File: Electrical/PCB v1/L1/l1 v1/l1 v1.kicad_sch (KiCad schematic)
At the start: 167 parts, among them J1 Conn_01x01_Socket, J2 Conn_01x01_Socket, SW1 SW_SPDT, U1 ESP32-S3-DEVKITM-1-N8, U2 LM2596ADJ

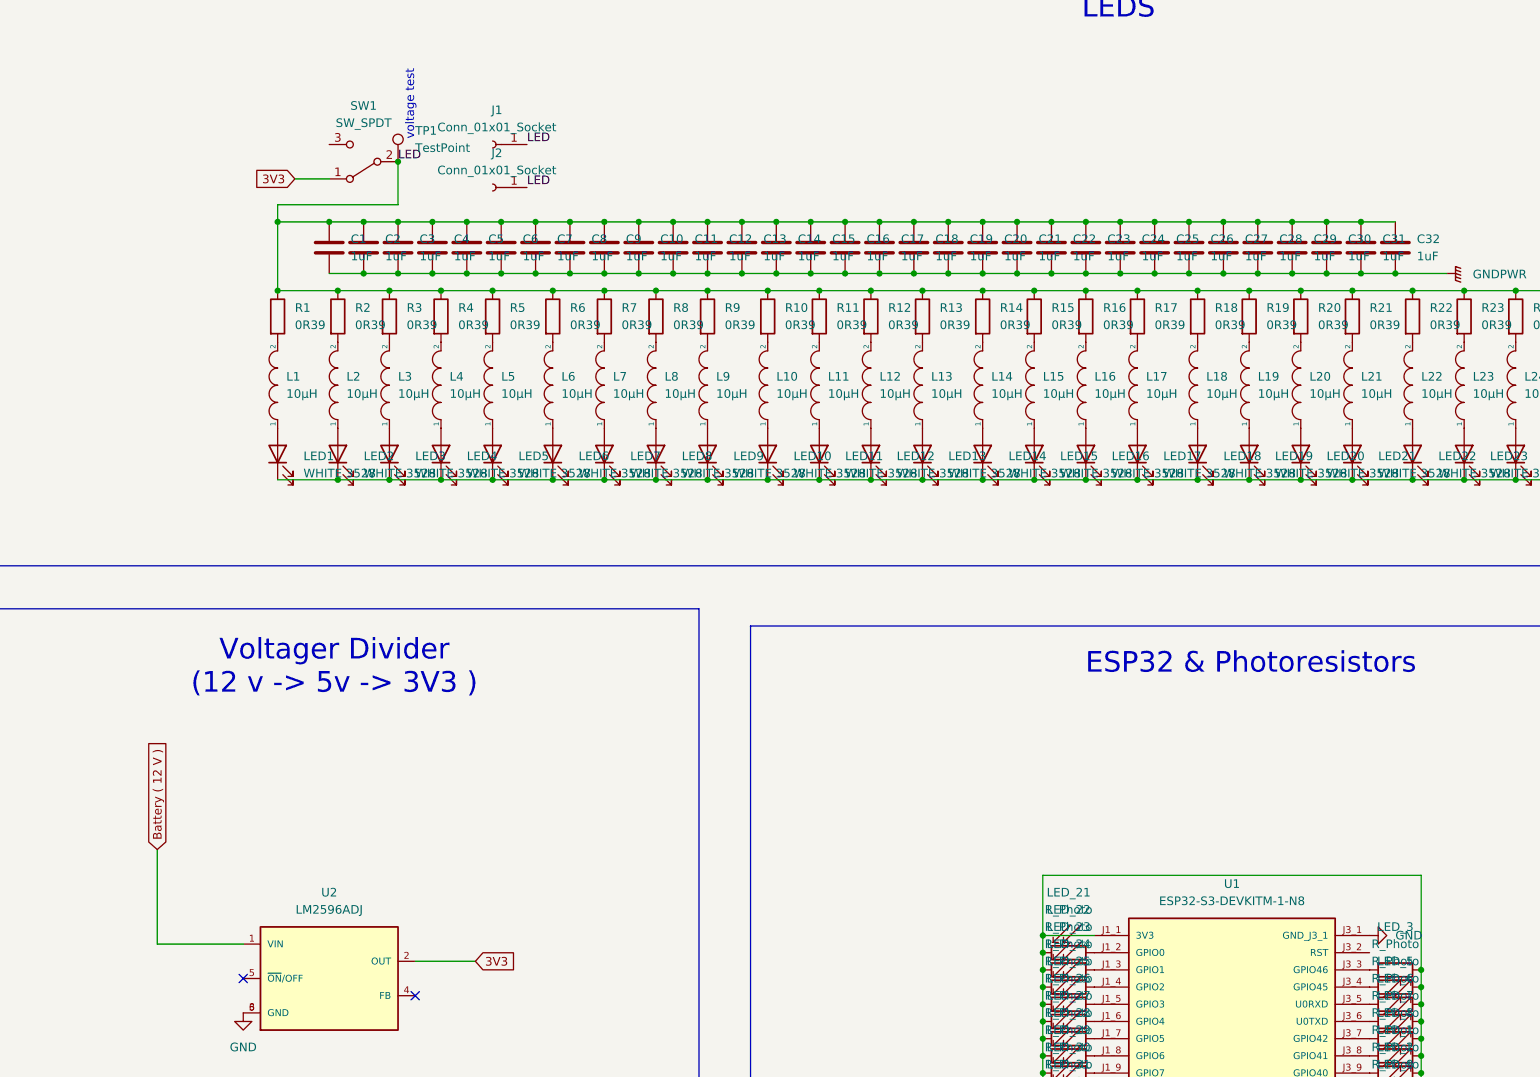
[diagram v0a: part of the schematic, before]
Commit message: renamed volatage divider to dc -dc converted for accurate naming, moved some text around becuz easier to read
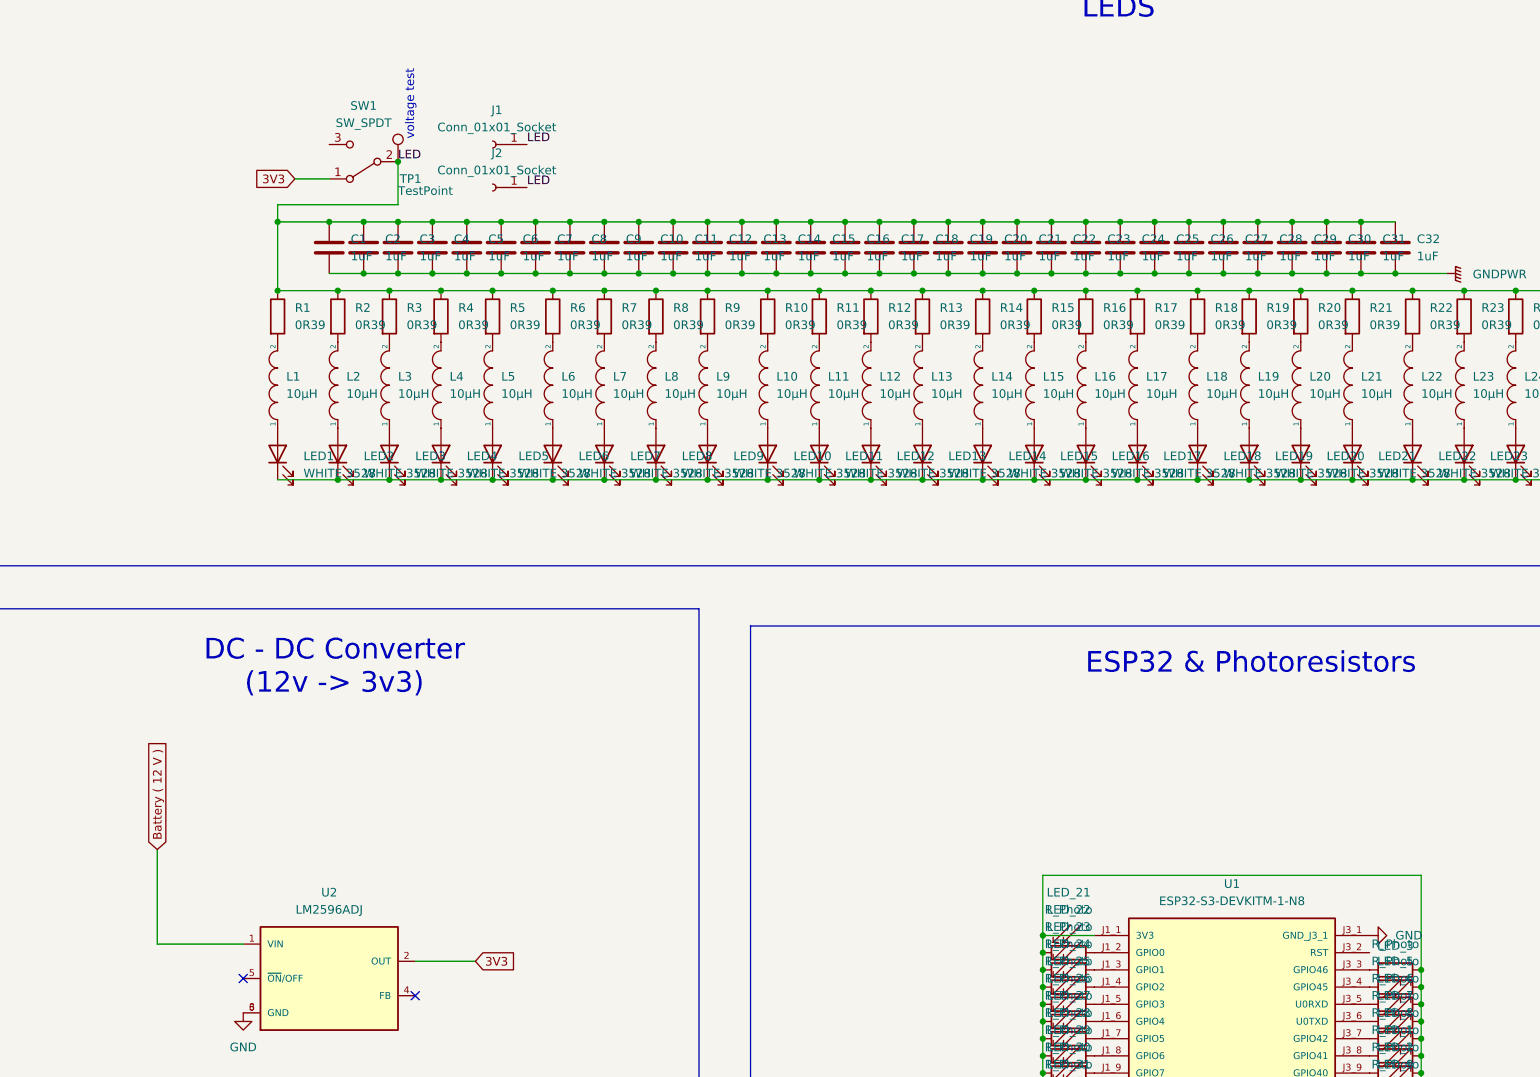
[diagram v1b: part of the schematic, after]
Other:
- note added: "DC - DC Converter (12v -> 3v3)"
- note removed: "Voltager Divider (12 v -> 5v -> 3V3 )"
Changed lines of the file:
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@@
 		)
 	)
-	(text "Voltager Divider \n(12 v -> 5v -> 3V3 )"
+	(text "DC - DC Converter \n(12v -> 3v3)"
 		(exclude_from_sim no)
 		(at 80.772 128.016 0)
@@
 		(on_board yes)
 		(dnp no)
-		(fields_autoplaced yes)
 		(property "Reference" "TP1"
-			(at 92.71 48.7679 0)
+			(at 90.424 55.88 0)
 			(effects
 				(font
@@
 		)
 		(property "Value" "TestPoint"
-			(at 92.71 51.3079 0)
+			(at 90.17 57.658 0)
 			(effects
 				(font
@@
 		(on_board yes)
 		(dnp no)
-		(fields_autoplaced yes)
 		(property "Reference" "LED_3"
-			(at 237.49 166.37 90)
+			(at 237.49 169.164 90)
 			(effects
 				(font
